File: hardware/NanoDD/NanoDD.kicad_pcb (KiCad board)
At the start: 2 copper layers, 41 x 10.2 mm, 33 parts, among them J1 Screw_Terminal_01x02, J2 Conn_01x06, J3 Screw_Terminal_01x02, Q1 AO3401A, Q2 AO3401A, U1 MSP430G2452IRSA16, U3 ZD24C128A-XGMB, U4 XC6206PxxxMR, U5 MS5607-02BA

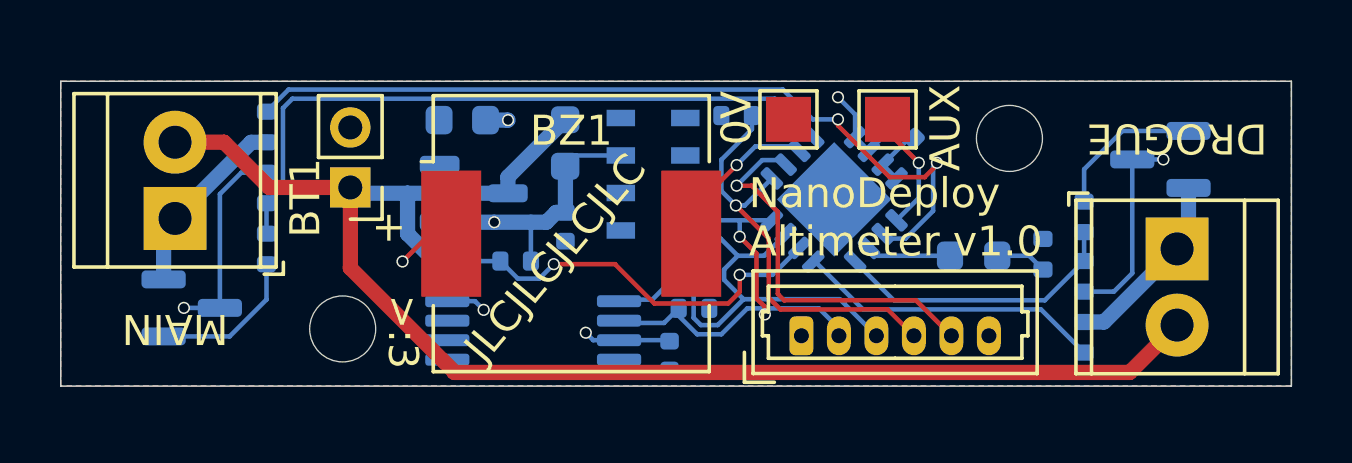
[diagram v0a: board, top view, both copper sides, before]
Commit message: Even more layout shrink, switch to barometer that's cheap on JLCPCB
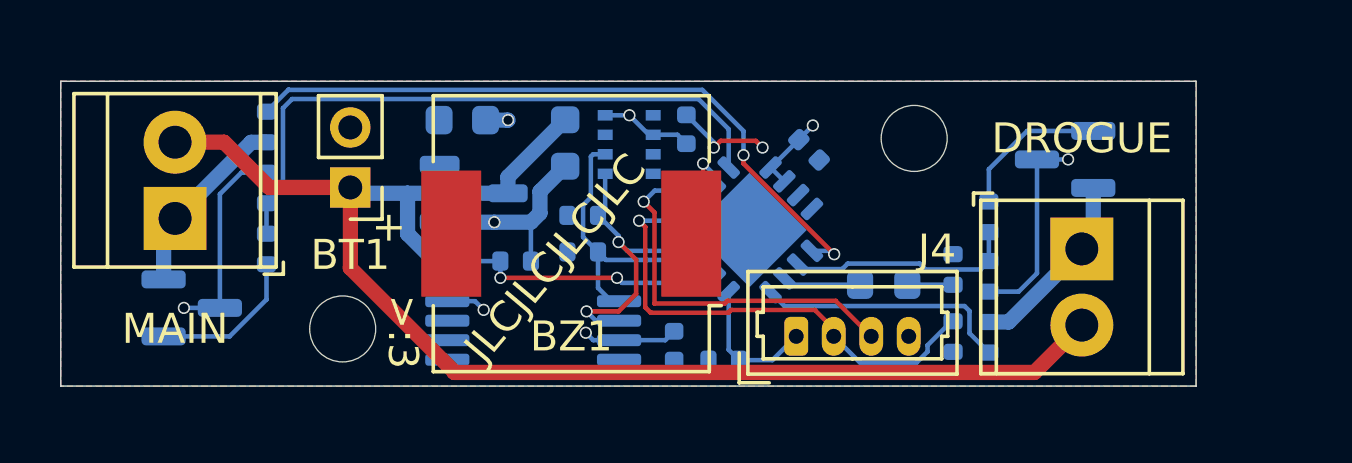
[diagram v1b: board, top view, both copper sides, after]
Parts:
- removed J2: Conn_01x06, Connector_Molex:Molex_PicoBlade_53047-0610_1x06_P1.25mm_Vertical
- removed TP1, TP2: TestPoint, TestPoint:TestPoint_Pad_1.5x1.5mm
- removed U5: MS5607-02BA, Package_LGA:LGA-8_3x5mm_P1.25mm
- added J4: Conn_01x04, Connector_Molex:Molex_PicoBlade_53047-0410_1x04_P1.25mm_Vertical, F.Cu at (177.3, 99.9)
- added R13: 4.7k, Resistor_SMD:R_0402_1005Metric, B.Cu at (174.9, 100.7)
- added U2: GZP6816D, Package_LGA:Bosch_LGA-8_2x2.5mm_P0.65mm_ClockwisePinNumbering, B.Cu at (171.7, 93.5)
- moved R5 10.3 mm to (182.5, 99.9), turned to 90 degrees
- moved C3 5.18 mm to (173.6, 93.0), turned to -90 degrees
- moved R7 4.83 mm to (170.2, 95.9), turned to 0 degrees
- moved R6 3.77 mm to (170.2, 97.1), turned to 0 degrees
- moved C1 3.25 mm to (177.7, 93.7)
- moved R1 3.18 mm to (183.7, 96.0)
- moved R2 3.18 mm to (183.7, 100.0)
- moved R3 3.18 mm to (183.7, 97.9)
- moved H2 3.17 mm to (181.2, 93.3)
- moved J3 3.17 mm to (186.8, 97.0)
- moved Q1 3.17 mm to (186.3, 94.0)
- moved D1 3.15 mm to (180.2, 98.2)
- moved R4 3.04 mm to (182.5, 97.7)
- moved U1 3.00 mm to (175.7, 96.4)
- moved C2 0.36 mm to (173.2, 100.3)
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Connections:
- BZ1 pad 1: +3.3V -> /BUZZER
- BZ1 pad 2: /BUZZER -> GND
- U1 pad 1: /AUX -> /CONT1
- U1 pad 2: /CONT1 -> /PYRO0
- U1 pad 4: /PYRO0 -> /CONT0
- U1 pad 5: /CONT0 -> /OWI
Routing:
- net /SCL: track 17.5 -> 9.82 mm
- net /SDA: track 15.9 -> 10.1 mm
- net /CONT1: track 28.0 -> 22.9 mm
- net /OWI: track 0.00 -> 4.86 mm
- net /VBAT_SENSE: track 13.2 -> 8.98 mm
- net /AUX: track 4.10 -> 0.00 mm, vias 1 -> 0
- net +BATT: track 50.6 -> 47.5 mm
- net /RST_TDIO: track 14.1 -> 16.7 mm
- net /BUZZER: track 5.33 -> 3.25 mm
- net /PYRO0: track 9.67 -> 7.66 mm
- net /CONT0: track 10.4 -> 8.70 mm
- net /PYRO1: track 22.7 -> 21.1 mm
- net +3.3V: track 4.07 -> 3.28 mm, vias 1 -> 2
- net /TEST_WTCK: track 12.9 -> 13.4 mm
- net GND: track 31.5 -> 31.4 mm, vias 7 -> 8
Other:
- board size 41 x 10.2 mm -> 37.8 x 10.2 mm
- board text removed: "0V"
- board text removed: "AUX"
- board text removed: "NanoDeploy Altimeter v1.0"

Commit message: Name and version badge on PCB
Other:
- board text added: "Nano Deploy"
- board text added: "v1.0"
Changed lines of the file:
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@@
+		)
+	)
+	(gr_text "v1.0\n"
+		(at 174.399 93.02 0)
+		(layer "F.SilkS")
+		(effects
+			(font
+				(size 1 1)
+				(thickness 0.1524)
+			)
+			(justify left bottom)
+		)
+	)
+	(gr_text "Nano\nDeploy"
+		(at 175.768 97.028 0)
+		(layer "F.SilkS")
+		(effects
+			(font
+				(size 1 1)
+				(thickness 0.1524)
+			)
+			(justify left bottom)
 		)
 	)

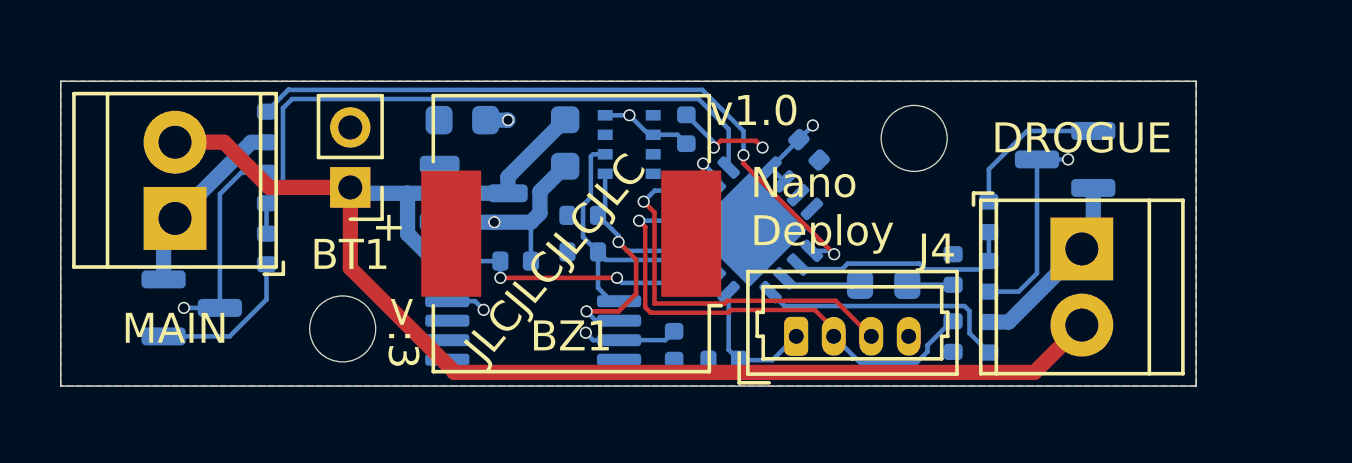
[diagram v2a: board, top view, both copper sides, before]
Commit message: Fixed swapped SCL/SDA
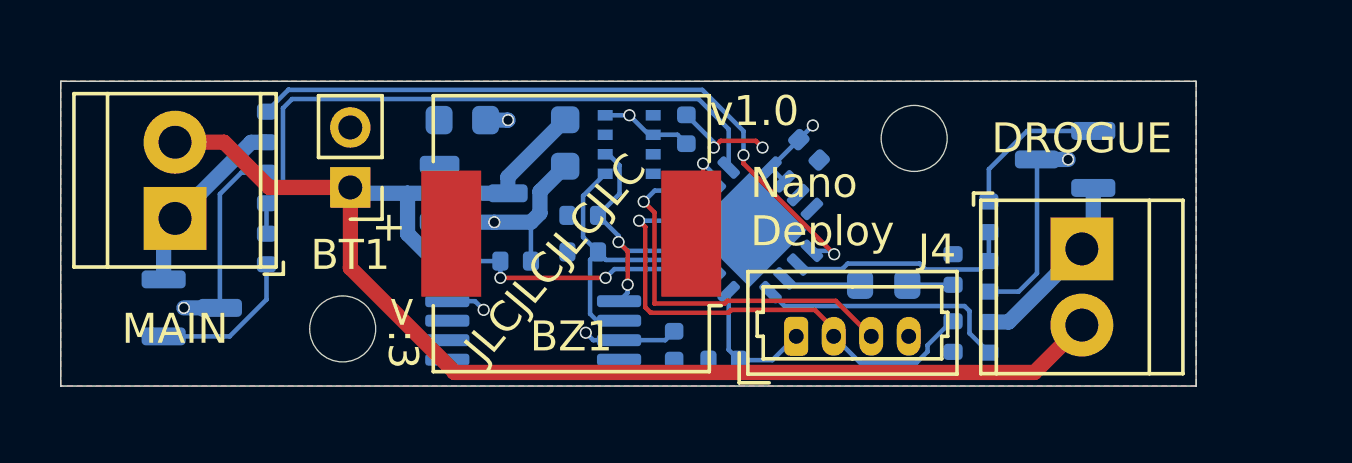
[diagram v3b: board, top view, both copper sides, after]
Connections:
- U2 pad 3: /SCL -> /SDA
- U2 pad 4: /SDA -> /SCL
- U3 pad 5: /SCL -> /SDA
- U3 pad 6: /SDA -> /SCL
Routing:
- net /SDA: track 10.1 -> 8.40 mm
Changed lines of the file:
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@@
 			(layers "B.Cu" "B.Paste" "B.Mask")
 			(roundrect_rratio 0.25)
-			(net 4 "/SCL")
+			(net 3 "/SDA")
 			(pinfunction "SDA")
 			(pintype "bidirectional")
@@
 			(layers "B.Cu" "B.Paste" "B.Mask")
 			(roundrect_rratio 0.25)
-			(net 3 "/SDA")
+			(net 4 "/SCL")
 			(pinfunction "SCL")
 			(pintype "input")
@@
 			(size 0.5 0.35)
 			(layers "B.Cu" "B.Paste" "B.Mask")
-			(net 4 "/SCL")
+			(net 3 "/SDA")
 			(pinfunction "SDA")
 			(pintype "bidirectional")
@@
 			(size 0.5 0.35)
 			(layers "B.Cu" "B.Paste" "B.Mask")
-			(net 3 "/SDA")
+			(net 4 "/SCL")
 			(pinfunction "SCL")
 			(pintype "input")
@@
 		(start 186.3598 94.046)
 		(end 185.323 94.046)
-		(width 0.1524)
+		(width 0.508)
 		(layer "B.Cu")
 		(net 1)
@@
 		(start 156.8856 98.994)
 		(end 158.085 98.994)
-		(width 0.1524)
+		(width 0.508)
 		(layer "B.Cu")
 		(net 1)
@@
 	)
 	(segment
-		(start 171.9608 97.3864)
-		(end 171.9608 98.5238)
-		(width 0.1524)
-		(layer "F.Cu")
-		(net 3)
-	)
-	(segment
-		(start 171.3738 99.1108)
-		(end 170.307 99.1108)
-		(width 0.1524)
-		(layer "F.Cu")
-		(net 3)
-	)
-	(segment
-		(start 171.9608 98.5238)
-		(end 171.3738 99.1108)
+		(start 171.6786 98.2218)
+		(end 171.6786 97.1042)
 		(width 0.1524)
 		(layer "F.Cu")
@@
 	)
 	(segment
-		(start 171.3738 96.7994)
-		(end 171.9608 97.3864)
+		(start 171.6786 97.1042)
+		(end 171.3738 96.7994)
 		(width 0.1524)
 		(layer "F.Cu")
@@
 	)
 	(via
-		(at 170.307 99.1108)
+		(at 171.3738 96.7994)
 		(size 0.4064)
 		(drill 0.3048)
@@
 	)
 	(via
-		(at 171.3738 96.7994)
+		(at 171.6786 98.2218)
 		(size 0.4064)
 		(drill 0.3048)
@@
 	)
 	(segment
-		(start 170.69 95.9104)
-		(end 170.9294 95.671)
+		(start 171.408 94.2428)
+		(end 171.0384 93.8732)
 		(width 0.1524)
 		(layer "B.Cu")
@@
 	)
 	(segment
-		(start 170.9294 95.671)
-		(end 170.9294 94.5232)
+		(start 171.6786 98.2218)
+		(end 171.6786 98.4837)
 		(width 0.1524)
 		(layer "B.Cu")
@@
 	)
 	(segment
-		(start 171.665668 97.091268)
-		(end 173.665474 97.091268)
+		(start 171.408 95.1924)
+		(end 171.408 94.2428)
 		(width 0.1524)
 		(layer "B.Cu")
@@
 	)
 	(segment
-		(start 171.3738 96.5942)
-		(end 170.69 95.9104)
+		(start 170.69 95.9104)
+		(end 171.408 95.1924)
 		(width 0.1524)
 		(layer "B.Cu")
@@
 	)
 	(segment
-		(start 170.617 99.4208)
-		(end 171.3915 99.4208)
+		(start 171.0384 93.8732)
+		(end 170.9294 93.8732)
 		(width 0.1524)
 		(layer "B.Cu")
@@
 	)
 	(segment
-		(start 171.3738 96.7994)
-		(end 171.3738 96.5942)
+		(start 171.6786 98.4837)
+		(end 171.3915 98.7708)
 		(width 0.1524)
 		(layer "B.Cu")
@@
 	)
 	(segment
-		(start 170.307 99.1108)
-		(end 170.617 99.4208)
+		(start 171.665668 97.091268)
+		(end 173.665474 97.091268)
 		(width 0.1524)
 		(layer "B.Cu")
@@
 	)
 	(segment
-		(start 173.06362 97.396068)
-		(end 170.956468 97.396068)
+		(start 171.3738 96.5942)
+		(end 170.69 95.9104)
 		(width 0.1524)
 		(layer "B.Cu")
-		(net 4)
+		(net 3)
 	)
 	(segment
-		(start 173.975216 97.700764)
-		(end 173.368316 97.700764)
+		(start 171.3738 96.7994)
+		(end 171.3738 96.5942)
 		(width 0.1524)
 		(layer "B.Cu")
-		(net 4)
+		(net 3)
 	)
 	(segment
-		(start 171.1354 98.7708)
-		(end 170.69 98.3254)
+		(start 170.4254 99.192199)
+		(end 170.4254 97.3942)
 		(width 0.1524)
 		(layer "B.Cu")
@@
 	)
 	(segment
-		(start 170.4508 93.9494)
-		(end 170.527 93.8732)
+		(start 173.06362 97.396068)
+		(end 170.956468 97.396068)
 		(width 0.1524)
 		(layer "B.Cu")
@@
 	)
 	(segment
-		(start 170.4508 95.3094)
-		(end 170.4508 93.9494)
+		(start 170.654001 99.4208)
+		(end 170.4254 99.192199)
 		(width 0.1524)
 		(layer "B.Cu")
@@
 	)
 	(segment
-		(start 170.69 97.1296)
-		(end 170.1914 96.631)
+		(start 173.975216 97.700764)
+		(end 173.368316 97.700764)
 		(width 0.1524)
 		(layer "B.Cu")
@@
 	)
 	(segment
-		(start 170.1914 96.631)
-		(end 170.1914 95.5688)
+		(start 171.3915 99.4208)
+		(end 170.654001 99.4208)
 		(width 0.1524)
 		(layer "B.Cu")
@@
 	)
 	(segment
-		(start 173.368316 97.700764)
-		(end 173.06362 97.396068)
+		(start 170.69 97.1296)
+		(end 170.1914 96.631)
 		(width 0.1524)
 		(layer "B.Cu")
@@
 	)
 	(segment
-		(start 170.527 93.8732)
-		(end 170.9294 93.8732)
+		(start 170.1914 95.2612)
+		(end 170.9294 94.5232)
 		(width 0.1524)
 		(layer "B.Cu")
@@
 	)
 	(segment
-		(start 174.125093 97.550887)
-		(end 173.975216 97.700764)
+		(start 170.4254 97.3942)
+		(end 170.69 97.1296)
 		(width 0.1524)
 		(layer "B.Cu")
@@
 	)
 	(segment
-		(start 170.956468 97.396068)
-		(end 170.69 97.1296)
+		(start 173.368316 97.700764)
+		(end 173.06362 97.396068)
 		(width 0.1524)
 		(layer "B.Cu")
@@
 	)
 	(segment
-		(start 171.3915 98.7708)
-		(end 171.1354 98.7708)
+		(start 174.125093 97.550887)
+		(end 173.975216 97.700764)
 		(width 0.1524)
 		(layer "B.Cu")
@@
 	)
 	(segment
-		(start 170.69 98.3254)
+		(start 170.956468 97.396068)
 		(end 170.69 97.1296)
 		(width 0.1524)
@@
 	)
 	(segment
-		(start 170.1914 95.5688)
-		(end 170.4508 95.3094)
+		(start 170.1914 96.631)
+		(end 170.1914 95.2612)
 		(width 0.1524)
 		(layer "B.Cu")
@@
 	)
 	(segment
-		(start 171.323 97.9932)
+		(start 170.942 97.9932)
 		(end 167.4368 97.9932)
 		(width 0.1524)
@@
 	)
 	(via
-		(at 171.323 97.9932)
+		(at 170.942 97.9932)
 		(size 0.4064)
 		(drill 0.3048)
@@
 	)
 	(segment
-		(start 174.584713 98.010507)
-		(end 174.434837 98.160383)
+		(start 172.937368 97.700868)
+		(end 173.396883 98.160383)
 		(width 0.1524)
 		(layer "B.Cu")
@@
 	)
 	(segment
-		(start 174.434837 98.160383)
-		(end 171.490183 98.160383)
+		(start 170.942 97.9932)
+		(end 171.234332 97.700868)
 		(width 0.1524)
 		(layer "B.Cu")
@@
 	)
 	(segment
-		(start 171.490183 98.160383)
-		(end 171.323 97.9932)
+		(start 171.234332 97.700868)
+		(end 172.937368 97.700868)
+		(width 0.1524)
+		(layer "B.Cu")
+		(net 12)
+	)
+	(segment
+		(start 174.434837 98.160383)
+		(end 174.584713 98.010507)
 		(width 0.1524)
 		(layer "B.Cu")
@@
 		(width 0.1524)
 		(layer "B.Cu")
+		(net 12)
+	)
+	(segment
+		(start 173.396883 98.160383)
+		(end 174.434837 98.160383)
+		(width 0.1524)
+		(layer "B.Cu")

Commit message: Correct MOSFETs and slightly better routing
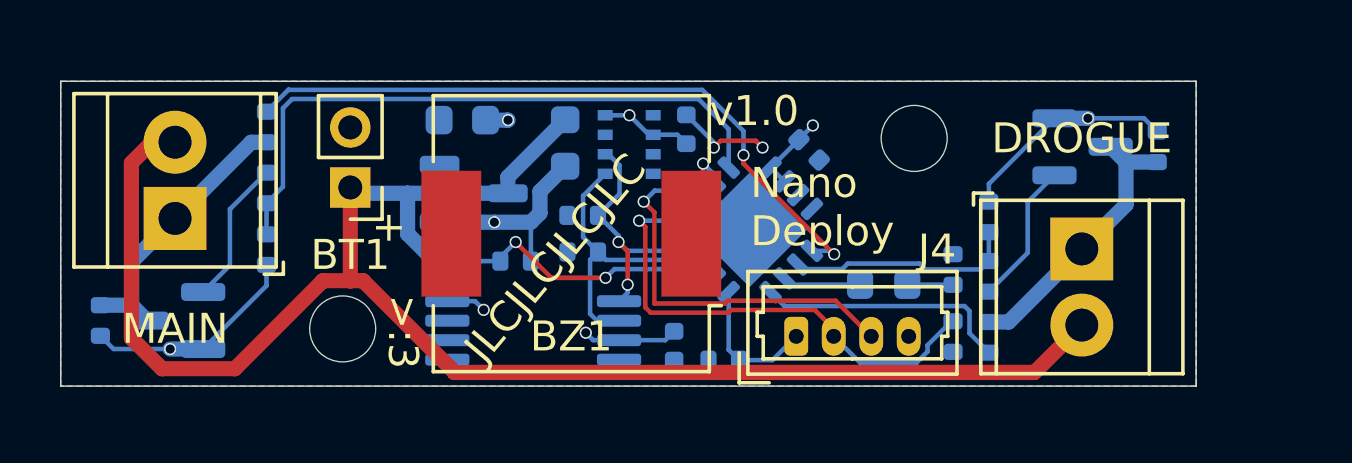
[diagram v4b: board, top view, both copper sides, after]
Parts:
- added R14: 47k, Resistor_SMD:R_0402_1005Metric, B.Cu at (154.1, 99.4)
- added R15: 47k, Resistor_SMD:R_0402_1005Metric, B.Cu at (189.3, 93.6)
- Q1, Q2: value AO3401A -> HL2302
- moved R11 2.06 mm to (159.6, 97.1), turned to -90 degrees
- moved R12 2.03 mm to (159.6, 95.0), turned to -90 degrees
- moved R1 1.98 mm to (183.7, 97.9), turned to 90 degrees
- moved R3 1.98 mm to (183.7, 96.0), turned to 90 degrees
- moved Q1 0.72 mm to (186.8, 93.6), turned to 0 degrees
- moved Q2 0.70 mm to (156.6, 99.4), turned to 180 degrees
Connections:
- Q1 pad 2: /EMATCH0 -> GND
- Q1 pad 3: GND -> /EMATCH0
- Q2 pad 2: /EMATCH1 -> GND
- Q2 pad 3: GND -> /EMATCH1
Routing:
- net +BATT: track 47.5 -> 57.7 mm
- net /EMATCH0: track 6.30 -> 9.37 mm
- net /EMATCH1: track 6.29 -> 9.36 mm
- net GND: track 31.4 -> 32.5 mm

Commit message: Ported to msp430-gcc because CCS on linux is bad
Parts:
- R1, R12, R4: value 270 -> 75
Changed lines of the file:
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@@
 			)
 		)
-		(property "Value" "270"
+		(property "Value" "75"
 			(at 0 -1.17 90)
 			(layer "B.Fab")
@@
 			)
 		)
-		(property "LCSC" "C25155"
+		(property "LCSC" "C25133"
 			(at 0 0 90)
 			(unlocked yes)
@@
 			)
 		)
+		(property "LCSC" "C28646268"
+			(at 0 0 180)
+			(unlocked yes)
+			(layer "B.Fab")
+			(hide yes)
+			(effects
+				(font
+					(size 1 1)
+					(thickness 0.15)
+				)
+				(justify mirror)
+			)
+		)
+		(property "JLCPCB_CORRECTION" "0;0;90"
+			(at 0 0 180)
+			(unlocked yes)
+			(layer "B.Fab")
+			(hide yes)
+			(effects
+				(font
+					(size 1 1)
+					(thickness 0.15)
+				)
+				(justify mirror)
+			)
+		)
 		(sheetname "Root")
 		(sheetfile "NanoDD.kicad_sch")
@@
 			)
 		)
-		(property "Value" "270"
+		(property "Value" "75"
 			(at 0 -1.17 90)
 			(layer "B.Fab")
@@
 			)
 		)
-		(property "LCSC" "C25155"
+		(property "LCSC" "C25133"
 			(at 0 0 -90)
 			(unlocked yes)
@@
 			)
 		)
-		(property "Value" "270"
+		(property "Value" "75"
 			(at 0 -1.17 90)
 			(layer "B.Fab")
@@
 			)
 		)
-		(property "LCSC" "C25155"
+		(property "LCSC" "C25133"
 			(at 0 0 90)
 			(unlocked yes)
@@
 		)
 		(property "Value" "HL2302"
-			(at 0 -2.4 360)
+			(at 0 -2.4 0)
 			(layer "B.Fab")
 			(effects
@@
 			)
 		)
+		(property "LCSC" "C28646268"
+			(at 0 0 0)
+			(unlocked yes)
+			(layer "B.Fab")
+			(hide yes)
+			(effects
+				(font
+					(size 1 1)
+					(thickness 0.15)
+				)
+				(justify mirror)
+			)
+		)
+		(property "JLCPCB_CORRECTION" "0;0;90"
+			(at 0 0 0)
+			(unlocked yes)
+			(layer "B.Fab")
+			(hide yes)
+			(effects
+				(font
+					(size 1 1)
+					(thickness 0.15)
+				)
+				(justify mirror)
+			)
+		)
 		(sheetname "Root")
 		(sheetfile "NanoDD.kicad_sch")
@@
 		)
 		(fp_text user "${REFERENCE}"
-			(at 0 0 360)
+			(at 0 0 0)
 			(layer "B.Fab")
 			(effects
